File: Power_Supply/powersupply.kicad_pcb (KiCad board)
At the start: 2 copper layers, 60.8 x 63.3 mm, 79 parts, among them J1 1x2, J101 USB_B_Micro, J102 Conn_01x03_Male, J103 Default_Jumper, J104 Default_Jumper, J2 1x2, Q1 IRF9Z24NPBF, SW1 KMR2, SW2 joystick-K1-1506DN-01, U101 AZ1117E-3.3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

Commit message: logo
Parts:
- added G***: LOGO, powersupply:Logo, B.Cu at (59.4, 65.3)

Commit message: small logo
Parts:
- moved G*** 3.56 mm to (59.4, 61.7)

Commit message: logo changes
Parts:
- moved G*** 13.0 mm to (59.6, 48.7)
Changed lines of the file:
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@@
-(kicad_pcb (version 20171130) (host pcbnew "(5.1.2-1)-1")
+(kicad_pcb (version 20171130) (host pcbnew "(5.1.4-0-10_14)")
   (general
     (thickness 1.6)
@@
   )
   (module powersupply:Logo (layer B.Cu)
-    (at 59.436 61.722 180)
+    (at 59.58 48.71 180)
     (fp_text reference G*** (at 0 0) (layer B.SilkS) hide
       (effects (font (size 1.524 1.524) (thickness 0.3)) (justify mirror))
@@
   (module powersupply:Default_Jumper (layer B.Cu)
     (at 55.594 34.29)
-    (fp_text reference J104 (at 0 2.5) (layer B.SilkS)
-      (effects (font (size 1 1) (thickness 0.15)) (justify mirror))
+    (fp_text reference J104 (at 0.016 1.39) (layer B.SilkS)
+      (effects (font (size 0.8 0.8) (thickness 0.15)) (justify mirror))
     )
     (fp_text value Default_Jumper (at 0 4.3) (layer B.Fab)
@@
   (module powersupply:Default_Jumper (layer B.Cu)
     (at 60.166 34.29)
-    (fp_text reference J103 (at 0 2.5) (layer B.SilkS)
-      (effects (font (size 1 1) (thickness 0.15)) (justify mirror))
+    (fp_text reference J103 (at 0.114 1.46) (layer B.SilkS)
+      (effects (font (size 0.8 0.8) (thickness 0.15)) (justify mirror))
     )
     (fp_text value Default_Jumper (at 0 4.3) (layer B.Fab)
@@
   (gr_arc (start 86.12 31.55) (end 89.57 31.55) (angle -90) (layer Edge.Cuts) (width 0.05))
   (gr_arc (start 32.27 87.95) (end 28.82 87.95) (angle -89.66785427) (layer Edge.Cuts) (width 0.05))
-  (gr_text "Variable\nPower Supply" (at 59.2 46.35) (layer B.SilkS)
+  (gr_text "Variable Power Supply" (at 60.1 37.95) (layer B.SilkS)
     (effects (font (size 2.5 2.5) (thickness 0.625)) (justify mirror))
   )

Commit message: bug 1/3
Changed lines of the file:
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@@
     (effects (font (size 1 1) (thickness 0.25)) (justify right))
   )
-  (gr_text - (at 64.13 89.98) (layer F.SilkS)
+  (gr_text - (at 54.92 90.07) (layer F.SilkS)
     (effects (font (size 1.5 1.5) (thickness 0.375)))
   )
-  (gr_text + (at 54.87 89.84) (layer F.SilkS)
+  (gr_text + (at 63.65 90) (layer F.SilkS)
     (effects (font (size 1.5 1.5) (thickness 0.375)))
   )

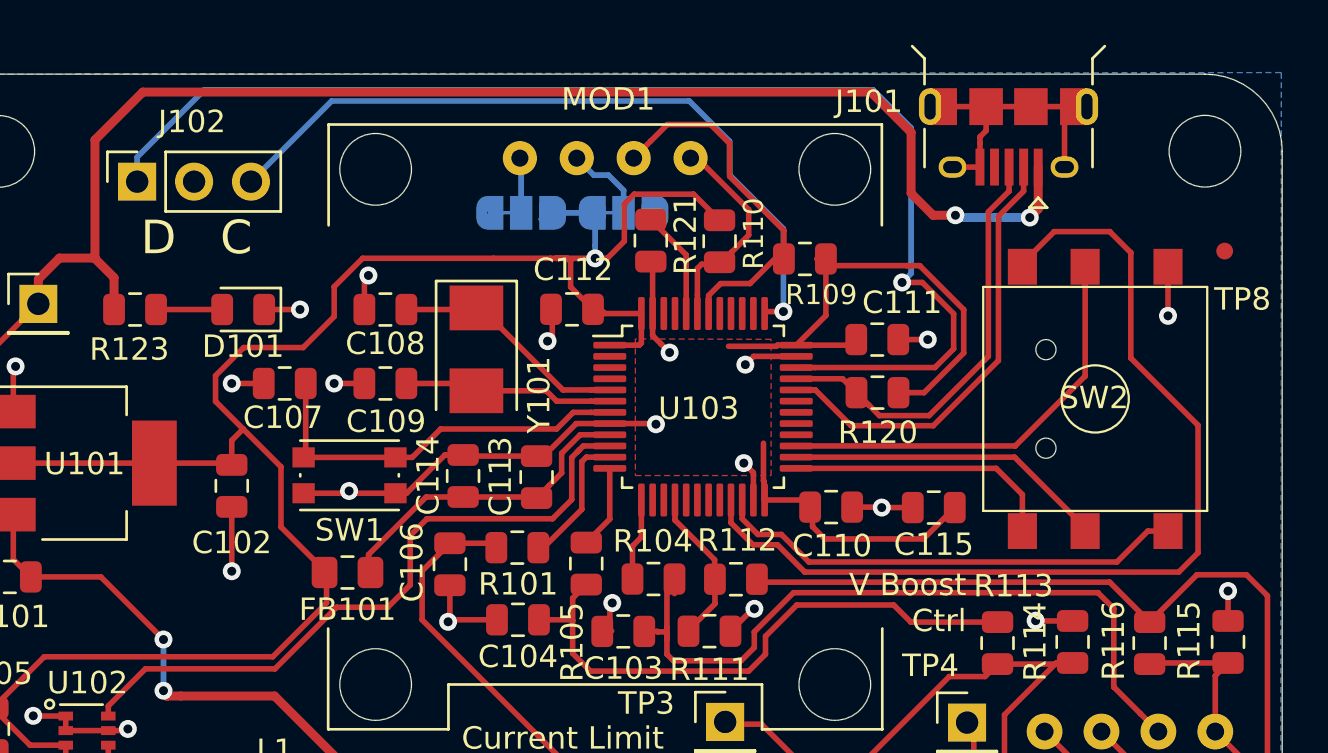
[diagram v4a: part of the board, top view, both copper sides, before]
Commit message: Fixed directional button (for real this time?)
Also laid out pullup resistor to make bootloader happy.
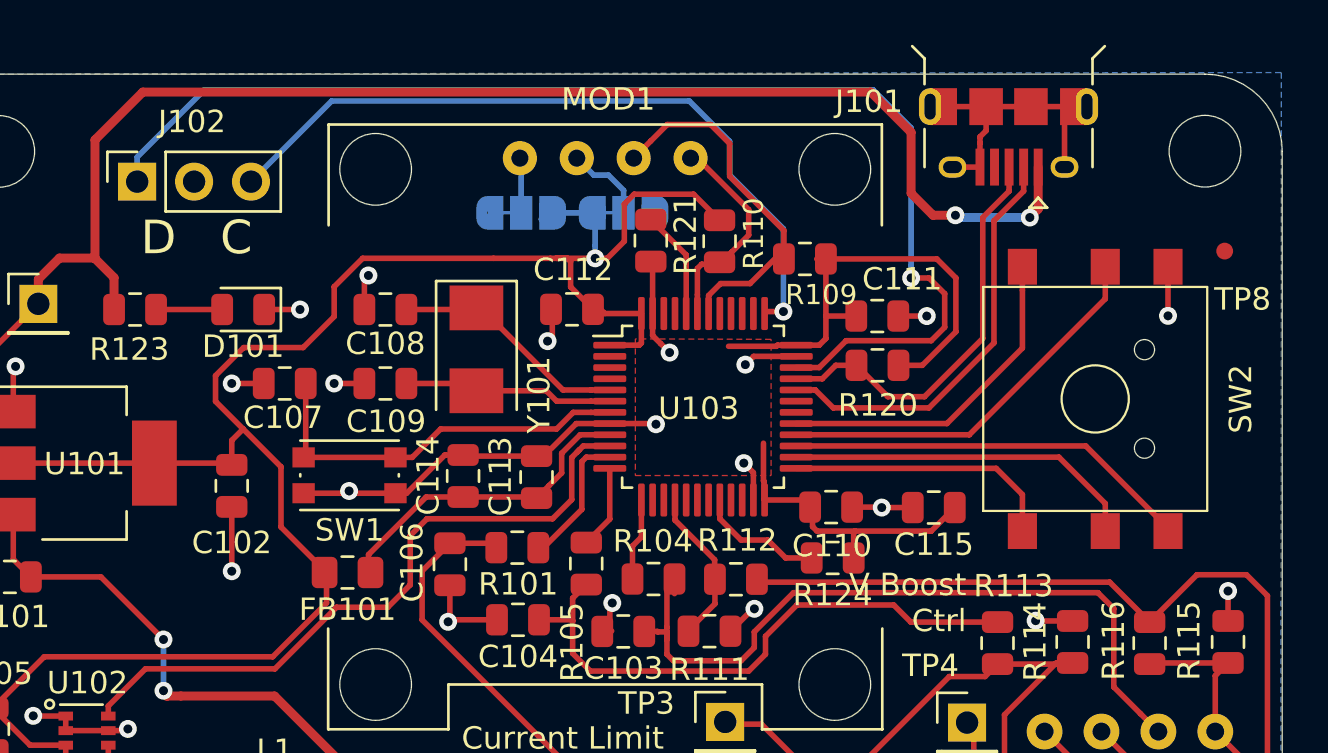
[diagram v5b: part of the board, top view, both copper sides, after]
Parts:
- removed G***: LOGO, powersupply:Logo
- added R124: 1.5k, Resistor_SMD:R_0805_2012Metric, F.Cu at (69.5, 49.7)
- moved R120 1.22 mm to (71.5, 41.1)
- moved C111 1.05 mm to (71.5, 38.9)
- turned SW2 to 270 degrees
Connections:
- SW2 pad 1: /up -> GND
- SW2 pad 2: /left -> /right
- SW2 pad 3: /down -> /center
- SW2 pad 4: GND -> /up
- SW2 pad 5: /right -> /left
- SW2 pad 6: /center -> /down
- U103 pad 21: /center -> Net-(U103-Pad21)
- U103 pad 22: /down -> Net-(U103-Pad22)
- U103 pad 27: /right -> /down
- U103 pad 28: Net-(U103-Pad28) -> /right
- U103 pad 29: Net-(U103-Pad29) -> /center
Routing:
- net /center: track 43.7 -> 15.1 mm
- net Net-(R124-Pad2): track 0.00 -> 5.66 mm
- net /down: track 21.2 -> 18.2 mm
- net /left: track 14.4 -> 15.9 mm
- net /SWDIO: track 56.5 -> 55.0 mm
- net /right: track 19.1 -> 17.7 mm
- net /D-: track 20.0 -> 18.8 mm
- net /D+: track 19.2 -> 18.4 mm
- net +3V3: track 154.1 -> 153.4 mm
